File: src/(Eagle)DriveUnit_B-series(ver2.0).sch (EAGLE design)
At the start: 68 parts, among them IC1 A3921, SW1 TVAF06-A020B-R, SW2 TVAF06-A020B-R, SW3 THAF01-NC-R, SW4 SS-12D00G3

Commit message: 配線の追加
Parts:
- removed R28: 100k, GF063P B104K:GF063PB104K
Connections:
- removed net N$16: R13.P$2, R28.RIGHT
- net GND: now also R13.P$2; no longer R28.LEFT
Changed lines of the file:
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@@
 <part name="SUPPLY20" library="supply2" library_urn="urn:adsk.eagle:library:372" deviceset="GND" device=""/>
 <part name="SUPPLY21" library="supply2" library_urn="urn:adsk.eagle:library:372" deviceset="GND" device=""/>
-<part name="R28" library="GF063P B104K" deviceset="GF063PB104K" device="" value="100k"/>
 </parts>
 <sheets>
@@
 <attribute name="VALUE" x="86.995" y="90.805" size="1.778" layer="96"/>
 </instance>
-<instance part="SUPPLY2" gate="GND" x="78.74" y="120.142" smashed="yes">
-<attribute name="VALUE" x="77.343" y="117.729" size="1.016" layer="96"/>
+<instance part="SUPPLY2" gate="GND" x="83.82" y="120.142" smashed="yes">
+<attribute name="VALUE" x="82.423" y="117.729" size="1.016" layer="96"/>
 </instance>
 <instance part="SUPPLY3" gate="GND" x="91.44" y="129.54" smashed="yes">
@@
 <instance part="R7" gate="G$1" x="114.3" y="55.88" smashed="yes" rot="R90"/>
 <instance part="R8" gate="G$1" x="139.7" y="55.88" smashed="yes" rot="R90"/>
-<instance part="R13" gate="G$1" x="94.742" y="124.46" smashed="yes"/>
+<instance part="R13" gate="G$1" x="92.202" y="124.46" smashed="yes"/>
 <instance part="R2" gate="G$1" x="91.44" y="139.7" smashed="yes" rot="R90"/>
 <instance part="R14" gate="G$1" x="91.44" y="154.94" smashed="yes" rot="R90"/>
@@
 <instance part="SUPPLY21" gate="GND" x="187.96" y="208.28" smashed="yes">
 <attribute name="VALUE" x="186.055" y="205.105" size="1.778" layer="96"/>
-</instance>
-<instance part="R28" gate="G$1" x="83.82" y="124.46" smashed="yes">
-<attribute name="NAME" x="81.788" y="125.7046" size="0.762" layer="95"/>
-<attribute name="VALUE" x="82.804" y="122.428" size="0.762" layer="96"/>
 </instance>
 </instances>
@@
 </segment>
 <segment>
-<pinref part="R28" gate="G$1" pin="LEFT"/>
+<pinref part="R13" gate="G$1" pin="P$2"/>
 <pinref part="SUPPLY2" gate="GND" pin="GND"/>
-<wire x1="78.74" y1="124.46" x2="78.74" y2="122.682" width="0.1524" layer="91"/>
+<wire x1="87.122" y1="124.46" x2="83.82" y2="124.46" width="0.1524" layer="91"/>
+<wire x1="83.82" y1="124.46" x2="83.82" y2="122.682" width="0.1524" layer="91"/>
 </segment>
 </net>
@@
 <pinref part="R13" gate="G$1" pin="P$1"/>
 <pinref part="IC1" gate="G$1" pin="RDEAD"/>
-<wire x1="99.822" y1="124.46" x2="101.6" y2="124.46" width="0.1524" layer="91"/>
-</segment>
-</net>
-<net name="N$16" class="0">
-<segment>
-<pinref part="R28" gate="G$1" pin="RIGHT"/>
-<pinref part="R13" gate="G$1" pin="P$2"/>
-<wire x1="88.9" y1="124.46" x2="89.662" y2="124.46" width="0.1524" layer="91"/>
-</segment>
-</net>
+<wire x1="97.282" y1="124.46" x2="101.6" y2="124.46" width="0.1524" layer="91"/>
+</segment>
+</net>

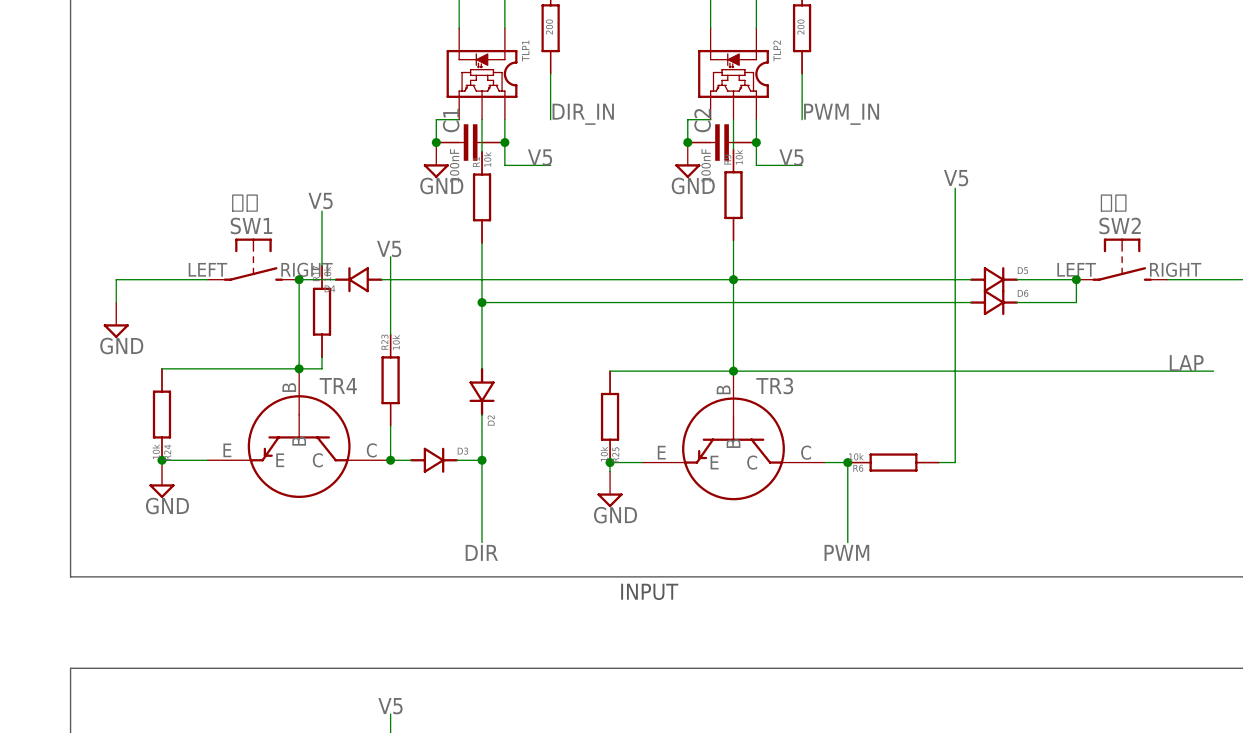
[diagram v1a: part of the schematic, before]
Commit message: 回路ミスってた(嘘だろ...)_KiCad以降前
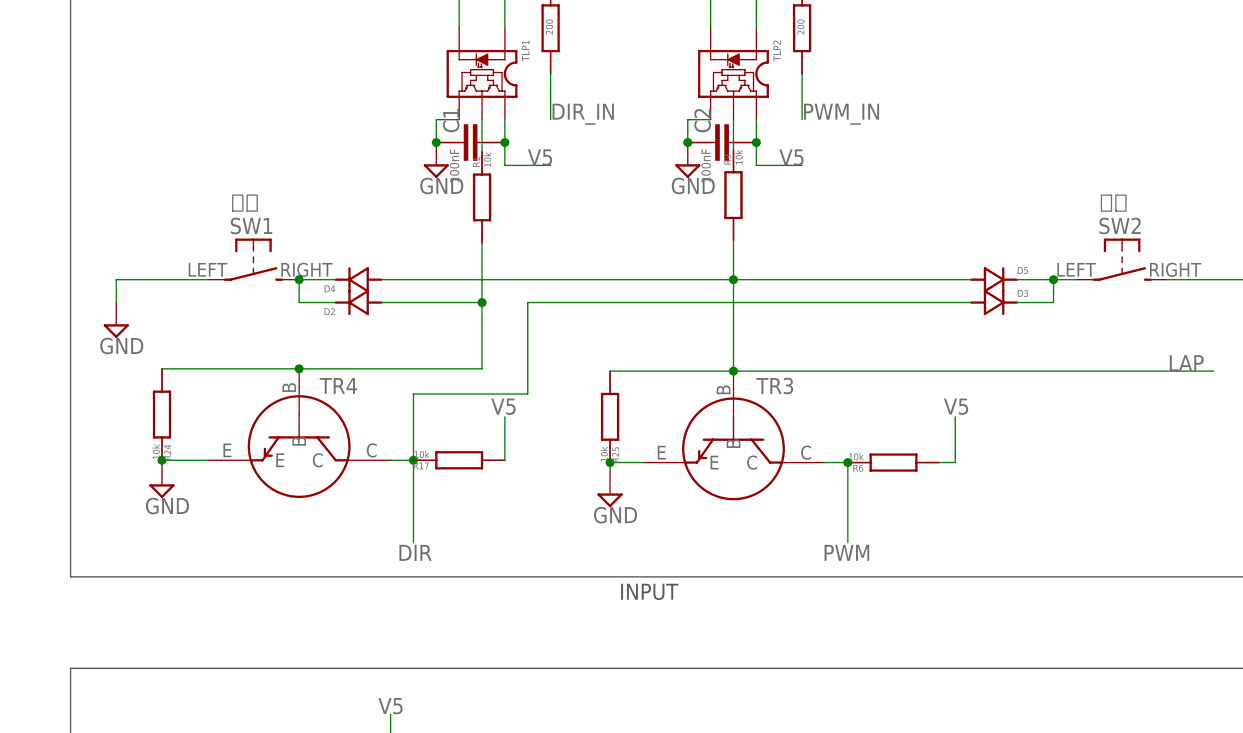
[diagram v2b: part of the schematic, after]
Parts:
- removed D6: GS1010FL, GS1010FL:GS1010FL
- removed R23: RG2012, RG2012:RG2012
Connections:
- removed net N$17: D4.C, R17.LEFT, R24.LEFT, SW1.S, TR4.B
- removed net N$27: D2.A, D6.A, R1.LEFT
- new net N$16: D2.A, R1.LEFT, R24.LEFT, TR4.B
- net DIR: now also D3.A, R17.RIGHT, TR4.C; no longer D2.C, D3.C
- net N$12: now also D2.C, D4.C, SW1.S; no longer D3.A, R23.LEFT, TR4.C
- net N$20: now also D3.C; no longer D6.C
- net V5: now also R17.LEFT; no longer R17.RIGHT, R23.RIGHT
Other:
- moved on the sheet: D2, D3, R17
